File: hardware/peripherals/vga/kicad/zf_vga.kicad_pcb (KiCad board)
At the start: 2 copper layers, 143 x 85 mm, 56 parts, among them J2 Z-FIGHTER Expansion Port, SW1 SW_DIP_x03, U1 4040, U10 74HC165, U11 AS6C6264, U12 74HC541, U13 74HC541, U14 74HC541, U2 4040, U3 GAL16V8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

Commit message: Routing
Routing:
- net CE2: track 105.3 -> 107.2 mm
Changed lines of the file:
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@@
     (thickness 1.6)
     (drawings 15)
-    (tracks 1042)
+    (tracks 1043)
     (zones 0)
     (modules 56)
@@
   (segment (start 193.691416 79.136416) (end 193.691416 90.491696) (width 0.1524) (layer F.Cu) (net 8))
   (segment (start 192.039 77.484) (end 193.691416 79.136416) (width 0.1524) (layer F.Cu) (net 8))
-  (via (at 220.768999 91.884) (size 0.6) (drill 0.3) (layers F.Cu B.Cu) (net 9))
-  (segment (start 221.068998 91.584001) (end 220.768999 91.884) (width 0.1524) (layer F.Cu) (net 9))
-  (segment (start 227.059 88.974) (end 223.678999 88.974) (width 0.1524) (layer F.Cu) (net 9))
-  (segment (start 223.678999 88.974) (end 221.068998 91.584001) (width 0.1524) (layer F.Cu) (net 9))
   (via (at 194.228999 93.334) (size 0.6) (drill 0.3) (layers F.Cu B.Cu) (net 9))
   (segment (start 192.439 74.944) (end 194.228999 76.733999) (width 0.1524) (layer F.Cu) (net 9))
   (segment (start 194.228999 76.733999) (end 194.228999 92.909736) (width 0.1524) (layer F.Cu) (net 9))
   (segment (start 194.228999 92.909736) (end 194.228999 93.334) (width 0.1524) (layer F.Cu) (net 9))
-  (segment (start 219.899 92.753999) (end 220.768999 91.884) (width 0.1524) (layer B.Cu) (net 9))
-  (segment (start 194.809 92.753999) (end 219.899 92.753999) (width 0.1524) (layer B.Cu) (net 9))
+  (via (at 220.768999 91.884) (size 0.6) (drill 0.3) (layers F.Cu B.Cu) (net 9))
   (segment (start 194.228999 93.334) (end 194.809 92.753999) (width 0.1524) (layer B.Cu) (net 9))
+  (segment (start 194.809 92.753999) (end 219.899 92.753999) (width 0.1524) (layer B.Cu) (net 9))
+  (segment (start 219.899 92.753999) (end 220.768999 91.884) (width 0.1524) (layer B.Cu) (net 9))
+  (segment (start 227.059 88.974) (end 223.678999 88.974) (width 0.1524) (layer F.Cu) (net 9))
+  (segment (start 223.678999 88.974) (end 221.068998 91.584001) (width 0.1524) (layer F.Cu) (net 9))
+  (segment (start 221.068998 91.584001) (end 220.768999 91.884) (width 0.1524) (layer F.Cu) (net 9))
   (via (at 212.15039 71.864) (size 0.6) (drill 0.3) (layers F.Cu B.Cu) (net 10))
   (segment (start 212.268999 71.864) (end 212.15039 71.864) (width 0.1524) (layer F.Cu) (net 10))
@@
   (segment (start 171.519 43.194) (end 174.840398 46.515398) (width 0.1524) (layer F.Cu) (net 76))
   (segment (start 118.219 95.264) (end 122.029 95.264) (width 0.1524) (layer B.Cu) (net 77))
-  (via (at 124.878999 60.193) (size 0.6) (drill 0.3) (layers F.Cu B.Cu) (net 77))
   (via (at 169.338999 60.193) (size 0.6) (drill 0.3) (layers F.Cu B.Cu) (net 77))
   (segment (start 169.338999 42.834001) (end 169.338999 60.283) (width 0.1524) (layer F.Cu) (net 77))
@@
   (segment (start 169.248999 60.193) (end 169.338999 60.283) (width 0.1524) (layer B.Cu) (net 77))
   (segment (start 124.659 60.193) (end 169.248999 60.193) (width 0.1524) (layer B.Cu) (net 77))
-  (segment (start 124.878999 92.414001) (end 122.029 95.264) (width 0.1524) (layer F.Cu) (net 77))
-  (segment (start 124.878999 60.193) (end 124.878999 92.414001) (width 0.1524) (layer F.Cu) (net 77))
+  (via (at 129.418999 60.194) (size 0.6) (drill 0.3) (layers F.Cu B.Cu) (net 77))
+  (segment (start 124.778999 64.834) (end 129.418999 60.194) (width 0.1524) (layer F.Cu) (net 77))
+  (segment (start 124.778999 92.514001) (end 124.778999 64.834) (width 0.1524) (layer F.Cu) (net 77))
+  (segment (start 122.029 95.264) (end 124.778999 92.514001) (width 0.1524) (layer F.Cu) (net 77))
   (segment (start 171.519 38.114) (end 168.719045 40.913955) (width 0.1524) (layer F.Cu) (net 78))
   (segment (start 168.719045 40.913955) (end 168.719045 49.92029) (width 0.1524) (layer F.Cu) (net 78))

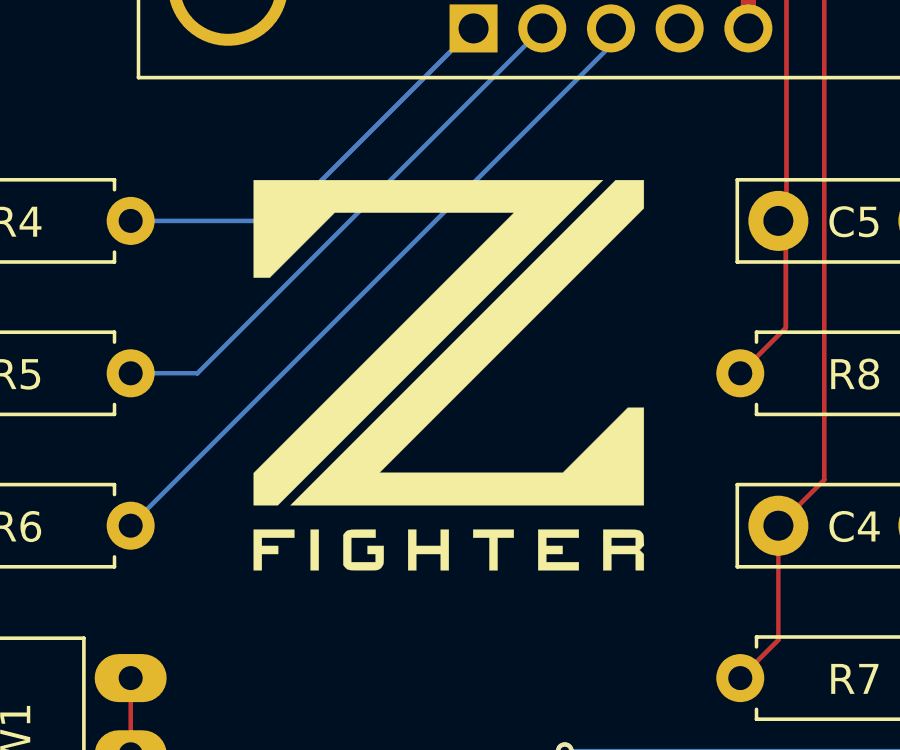
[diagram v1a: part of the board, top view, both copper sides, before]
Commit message: Silkscreen tweak
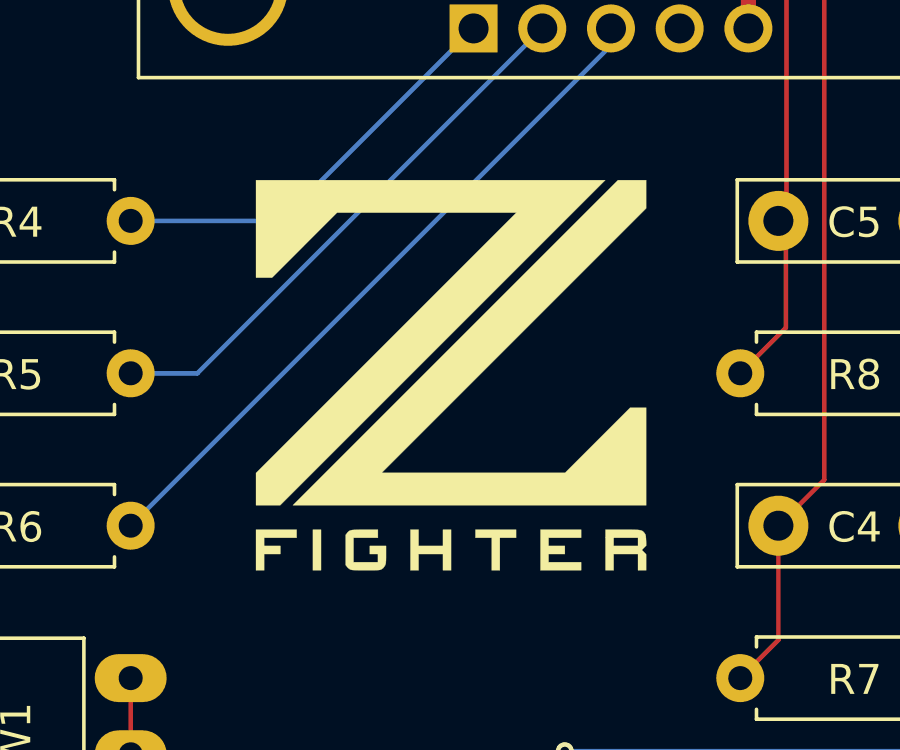
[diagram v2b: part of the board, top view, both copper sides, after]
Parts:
- moved G*** 0.08 mm to (108.5, 48.3)

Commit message: Routing
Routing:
- net VCC: track 82.7 -> 80.1 mm
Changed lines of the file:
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@@
     (thickness 1.6)
     (drawings 15)
-    (tracks 1043)
+    (tracks 1042)
     (zones 0)
     (modules 56)
@@
   (segment (start 146.05 92.699) (end 147.345 93.994) (width 0.508) (layer F.Cu) (net 20))
   (segment (start 90.239 87.644) (end 90.239 90.159) (width 0.508) (layer F.Cu) (net 20))
-  (segment (start 133.419 43.194) (end 133.419 45.734) (width 0.508) (layer F.Cu) (net 20))
   (segment (start 209.619 55.894) (end 210.889 57.164) (width 0.508) (layer F.Cu) (net 20))
   (segment (start 227.119 50.814) (end 222.748999 50.814) (width 1.5) (layer B.Cu) (net 20))
@@
   (segment (start 209.619 73.674) (end 209.489 73.804) (width 0.1524) (layer B.Cu) (net 49))
   (segment (start 209.489 73.804) (end 188.778999 73.804) (width 0.1524) (layer B.Cu) (net 49))
-  (segment (start 146.119 35.574) (end 143.288999 35.574) (width 0.1524) (layer B.Cu) (net 50))
-  (segment (start 142.028999 36.834) (end 134.699 36.834) (width 0.1524) (layer B.Cu) (net 50))
-  (segment (start 143.288999 35.574) (end 142.028999 36.834) (width 0.1524) (layer B.Cu) (net 50))
-  (segment (start 134.699 36.834) (end 133.419 38.114) (width 0.1524) (layer B.Cu) (net 50))
   (segment (start 175.57039 37.08539) (end 179.139 40.654) (width 0.1524) (layer B.Cu) (net 50))
   (segment (start 160.456389 37.08539) (end 175.57039 37.08539) (width 0.1524) (layer B.Cu) (net 50))
@@
   (segment (start 180.17761 41.69261) (end 179.139 40.654) (width 0.1524) (layer B.Cu) (net 50))
   (segment (start 191.839 43.194) (end 190.3376 41.6926) (width 0.1524) (layer B.Cu) (net 50))
+  (segment (start 146.119 35.574) (end 143.288999 35.574) (width 0.1524) (layer B.Cu) (net 50))
+  (segment (start 143.288999 35.574) (end 142.028999 36.834) (width 0.1524) (layer B.Cu) (net 50))
+  (segment (start 142.028999 36.834) (end 134.699 36.834) (width 0.1524) (layer B.Cu) (net 50))
+  (segment (start 134.699 36.834) (end 133.419 38.114) (width 0.1524) (layer B.Cu) (net 50))
   (via (at 186.278999 37.633995) (size 0.6) (drill 0.3) (layers F.Cu B.Cu) (net 51))
   (segment (start 184.219 35.574) (end 186.278995 37.633995) (width 0.1524) (layer F.Cu) (net 51))

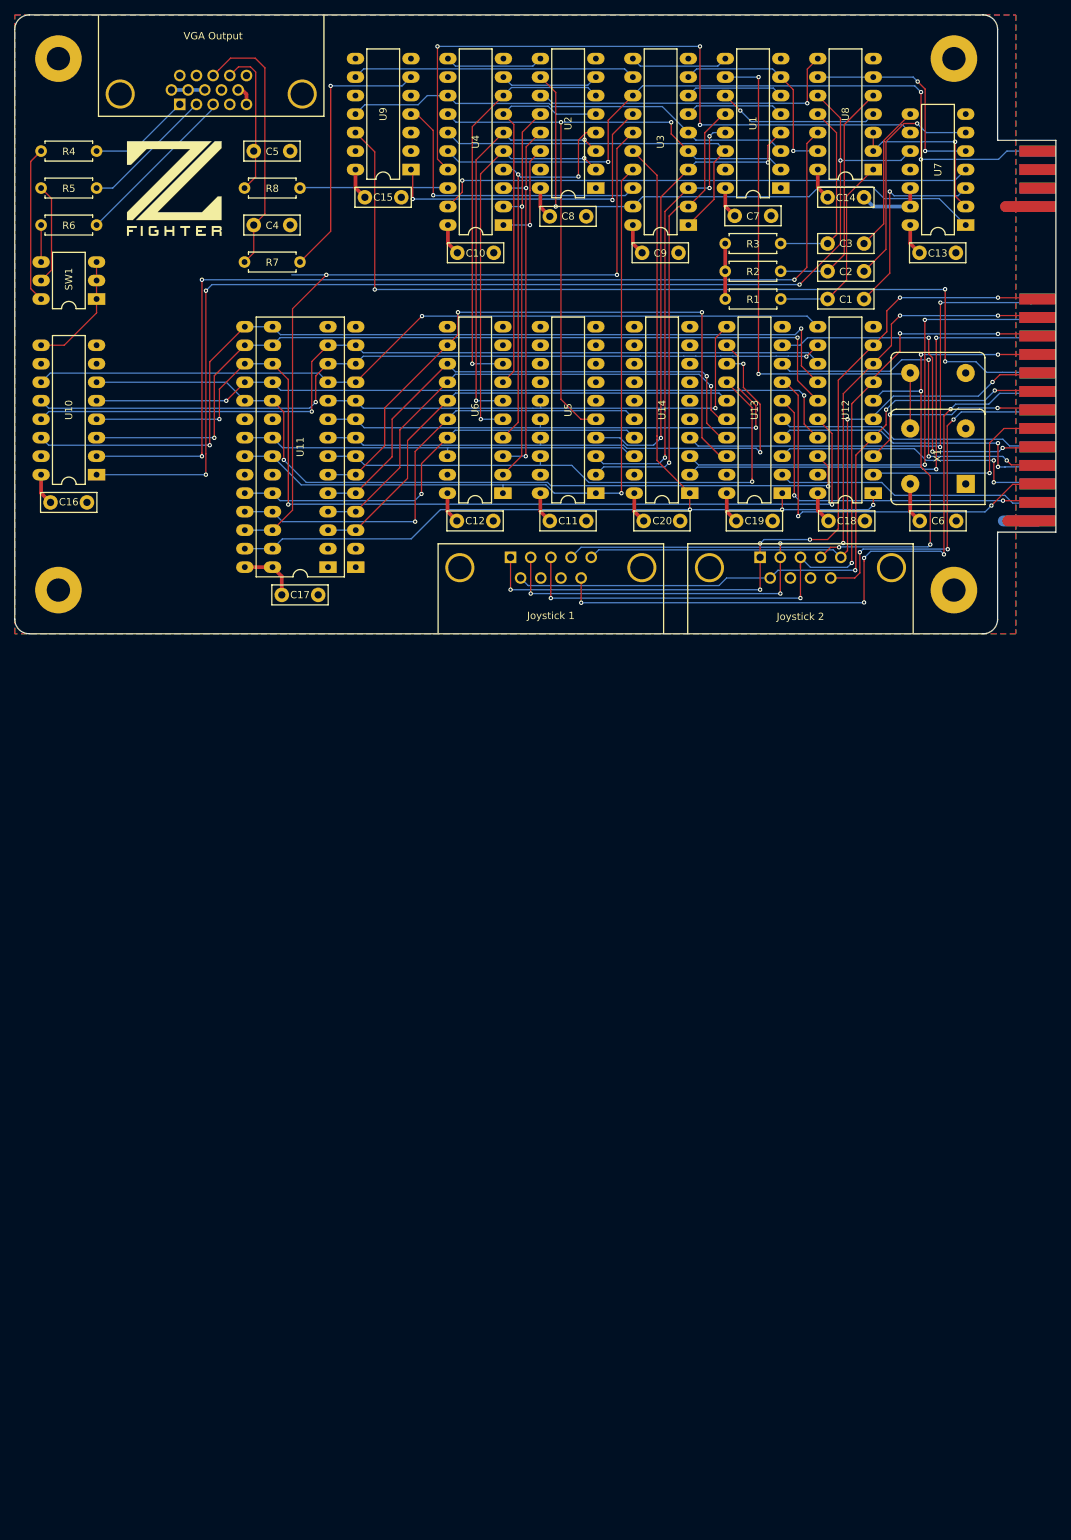
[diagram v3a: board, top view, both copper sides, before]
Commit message: Reduced pins of SRAM footprint
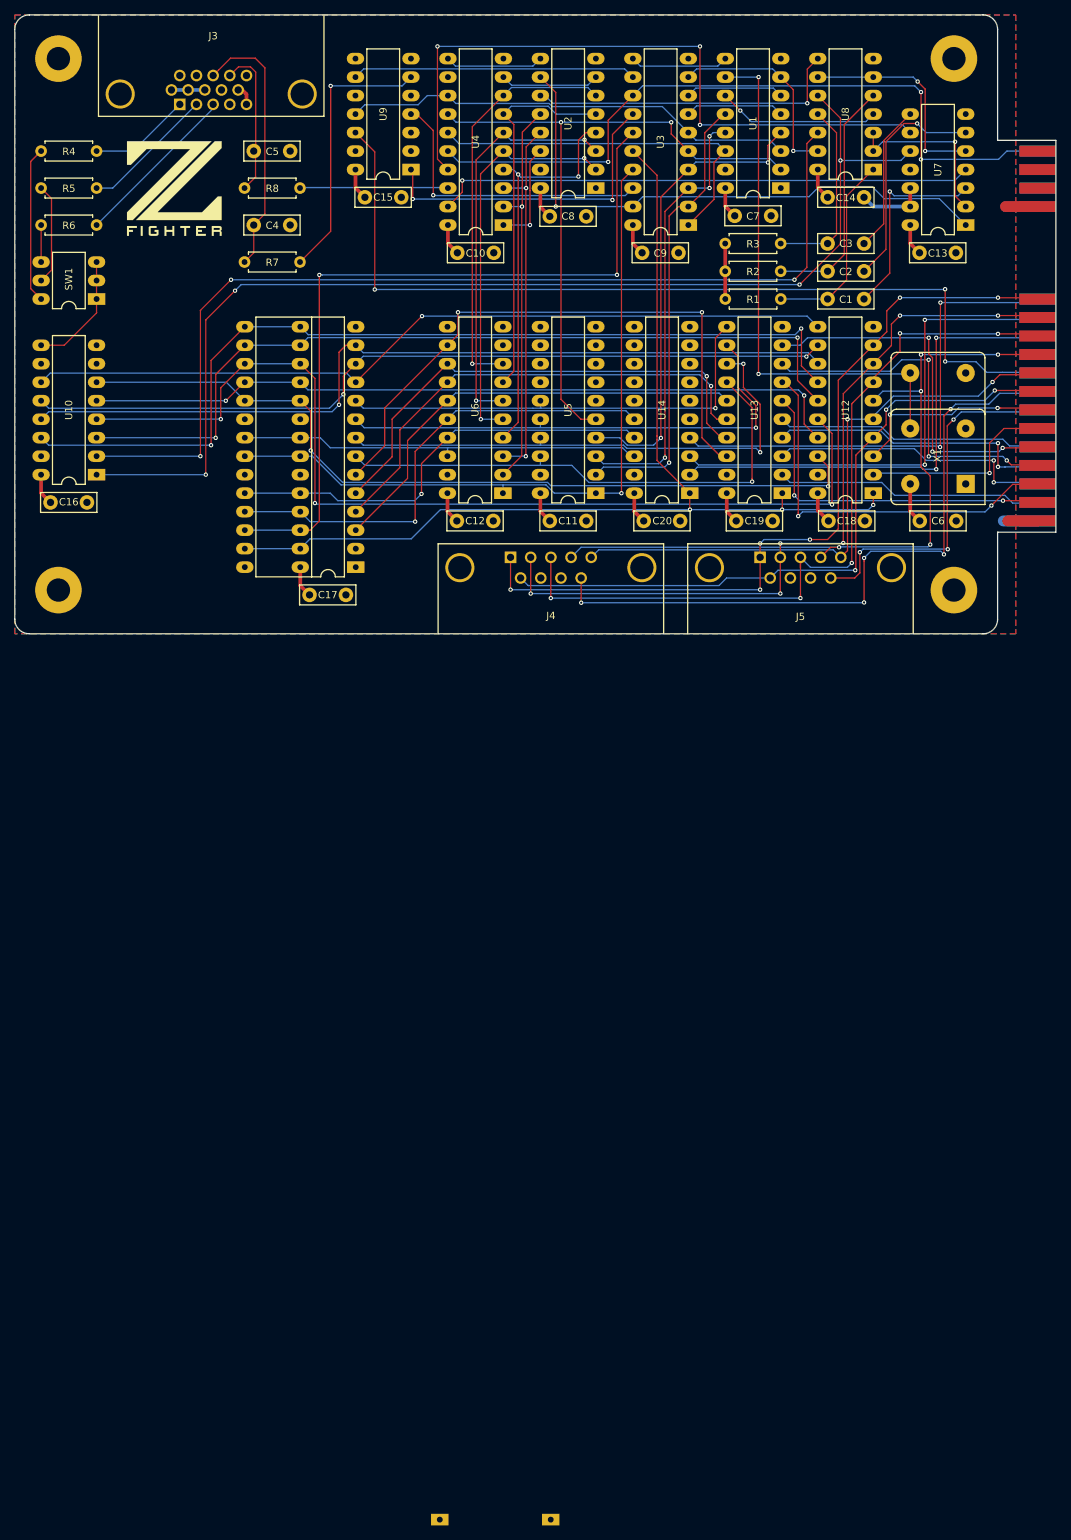
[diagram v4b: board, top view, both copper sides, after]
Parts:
- removed the U11 at (129.6, 100.3)
- removed the U11 at (133.5, 100.3)
- added ?: , , F.Cu at (72.5, 130.8)
- added ?: , , F.Cu at (87.7, 130.8)
- added U11: AS6C6264, Package_DIP:DIP-28_W7.62mm_LongPads, F.Cu at (133.5, 100.3)
- J3: renamed from VGA Output
- J4: renamed from Joystick 1
- J5: renamed from Joystick 2
- moved C17 3.81 mm to (127.1, 104.2)
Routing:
- net VCC: track 80.1 -> 76.3 mm
- net A7: track 66.0 -> 62.2 mm
- net A5: track 73.2 -> 69.4 mm
- net A4: track 87.1 -> 83.3 mm
- net A3: track 76.2 -> 72.3 mm
- net A2: track 76.7 -> 72.9 mm
- net A1: track 73.3 -> 69.5 mm
- net A0: track 66.5 -> 62.7 mm
- net A6: track 70.1 -> 66.5 mm
- net #P1: track 141.6 -> 139.1 mm
- net #LDPULSE: track 161.9 -> 159.5 mm
- net CE2: track 107.2 -> 106.0 mm
- net D7: track 115.0 -> 114.3 mm
- net D1: track 112.8 -> 112.2 mm
- net GND: track 34.6 -> 35.1 mm

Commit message: Silkscreen fixes
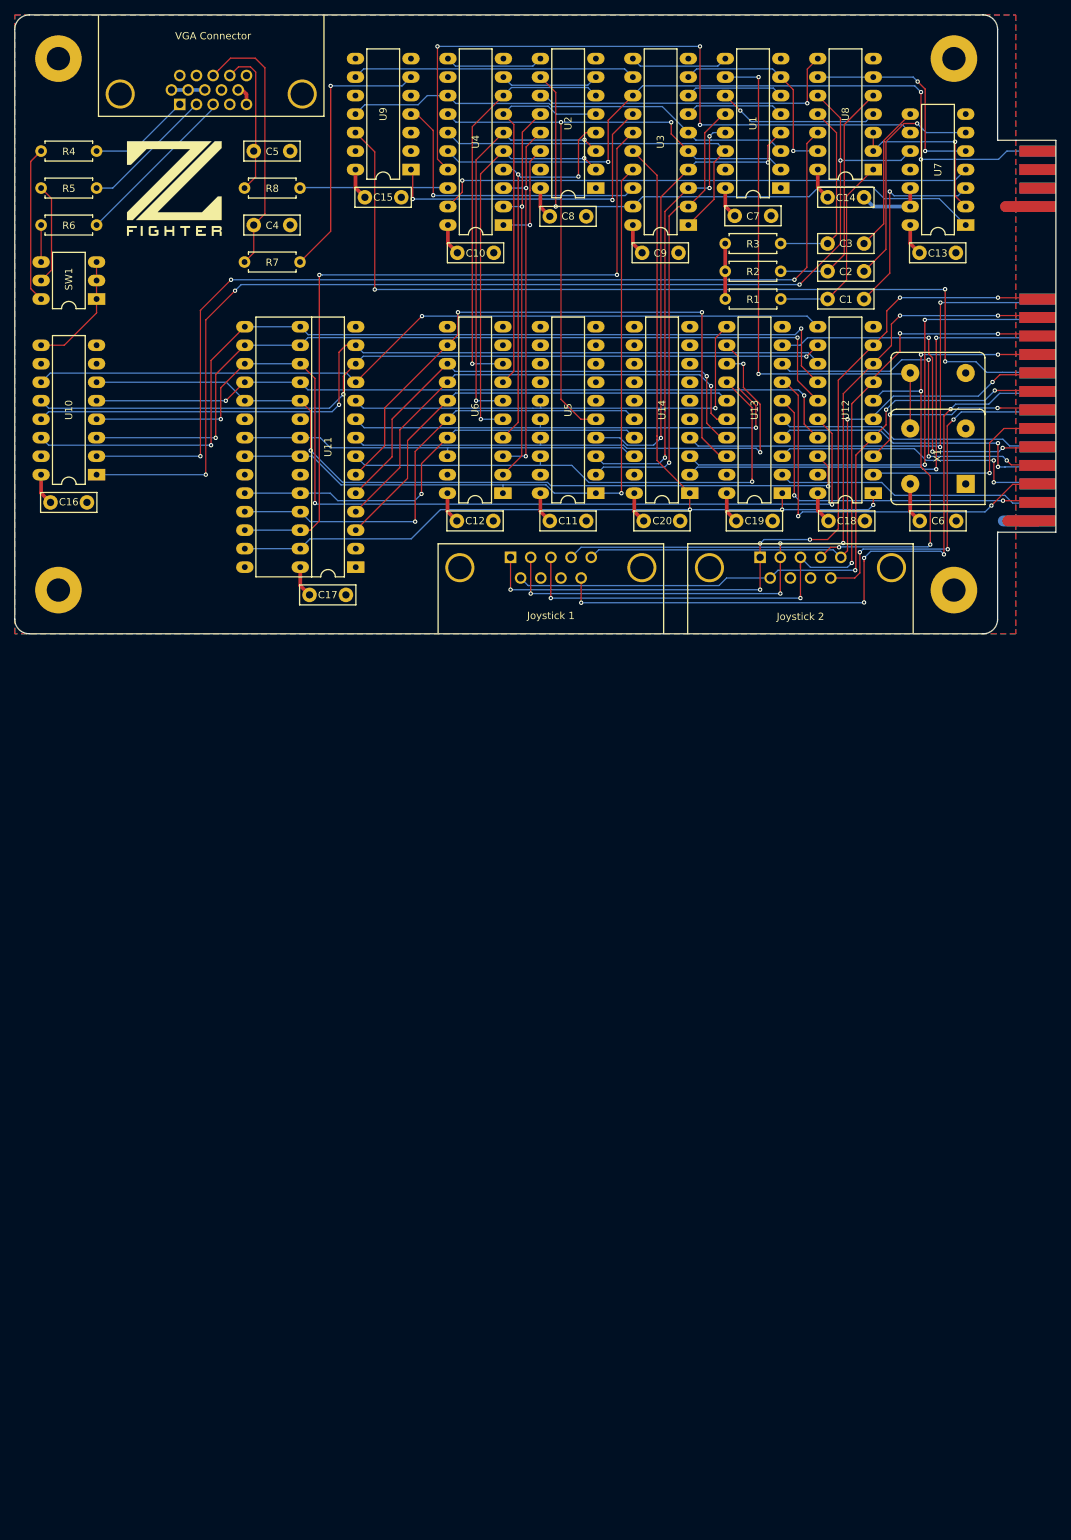
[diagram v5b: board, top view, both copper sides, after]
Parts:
- removed ? (x2): , 
- Joystick 1: renamed from J4
- Joystick 2: renamed from J5
- VGA Connector: renamed from J3

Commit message: Routing tweaks
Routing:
- net A0: track 62.7 -> 61.9 mm
- net A6: track 66.5 -> 65.7 mm
- net CE2: track 106.0 -> 105.2 mm
- net A4: track 83.3 -> 82.8 mm

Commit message: Fixed SRAM decoupling
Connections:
- U11 pad 28: VCC -> (no net)
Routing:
- net (no net): track 0.00 -> 12.0 mm
- net VCC: track 76.3 -> 72.0 mm
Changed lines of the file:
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@@
     (thickness 1.6)
     (drawings 15)
-    (tracks 1020)
+    (tracks 1021)
     (zones 0)
     (modules 55)
@@
     (mod_text_size 1 1)
     (mod_text_width 0.15)
-    (pad_size 2.4 1.6)
-    (pad_drill 0.8)
+    (pad_size 2 2)
+    (pad_drill 1)
     (pad_to_mask_clearance 0)
     (aux_axis_origin 0 0)
@@
       (net 113 D4))
     (pad 28 thru_hole oval (at 15.24 0 180) (size 2.4 1.6) (drill 0.8) (layers *.Cu *.Mask)
-      (net 20 VCC) (zone_connect 1))
+      (zone_connect 1))
     (pad 23 thru_hole oval (at 15.24 12.7 180) (size 2.4 1.6) (drill 0.8) (layers *.Cu *.Mask)
       (net 7 GND))
@@
       (net 7 GND))
     (pad 28 thru_hole oval (at 7.62 0 180) (size 2.4 1.6) (drill 0.8) (layers *.Cu *.Mask)
-      (net 20 VCC) (zone_connect 0))
+      (zone_connect 0))
     (model ${KISYS3DMOD}/Package_DIP.3dshapes/DIP-28_W7.62mm.wrl
       (at (xyz 0 0 0))
@@
   (segment (start 146.119 55.869) (end 147.414 57.164) (width 0.508) (layer F.Cu) (net 20))
   (segment (start 209.619 53.354) (end 209.438999 53.534001) (width 0.508) (layer B.Cu) (net 20))
-  (segment (start 125.839 102.884) (end 127.109 104.154) (width 0.508) (layer F.Cu) (net 20))
-  (segment (start 125.839 100.344) (end 125.839 102.884) (width 0.508) (layer F.Cu) (net 20))
+  (segment (start 125.839 102.884) (end 127.109 104.154) (width 0.508) (layer F.Cu) (net 0))
+  (segment (start 125.839 100.344) (end 125.839 102.884) (width 0.508) (layer F.Cu) (net 0))
+  (segment (start 125.839 100.344) (end 118.219 100.344) (width 0.508) (layer B.Cu) (net 0))
   (segment (start 227.029 91.544) (end 227.119 91.454) (width 0.1524) (layer B.Cu) (net 21))
   (segment (start 223.688999 91.544) (end 227.029 91.544) (width 0.1524) (layer B.Cu) (net 21))

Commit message: Routing
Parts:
- moved G*** 1.41 mm to (107.5, 97.3)
